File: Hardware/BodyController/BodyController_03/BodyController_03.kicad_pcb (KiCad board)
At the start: 4 copper layers, 154.9 x 116.8 mm, 332 parts, among them J1 7807, J10 7807, J11 7807, J2 CONN_01X08, J3 CONN_01X06, J5 CONN_01X14, J6 CONN_01X02, J7 CONN_01X06, J8 USB_OTG, J9 CONN_01X14, Q1 NX1029X,115, Q10 NX1029X,115, Q11 NX1029X,115, Q12 BUK9Y3R0-40E,115, Q13 BUK9Y3R0-40E,115, Q14 BUK9Y3R0-40E,115, Q15 2N7002, Q16 2N7002, Q2 NX1029X,115, Q3 BUK9Y3R0-40E,115, Q4 BUK9Y3R0-40E,115, Q5 BUK9Y3R0-40E,115, Q6 NX1029X,115, Q7 NX1029X,115, Q8 2N7002, Q9 2N7002, U1 PIC33EPxxxMU810, U10 BTS50202EKAXUMA2, U11 BTS50202EKAXUMA2, U12 BTS50202EKAXUMA2, U13 BTS50202EKAXUMA2, U14 BTS50202EKAXUMA2, U15 BTS716G, U16 MCP2562-H/SN, U17 OPA320-Q1, U18 TLV70033DDC, U19 TLV70033DDC, U2 LM2903QDRQ1, U20 LMR140x0, U21 LM2903QDRQ1, U22 UCC27511A-Q1, U23 tps25940-q1, U25 UCC27511A-Q1, U27 INA21x, U28 OPA320-Q1, U29 FT230X, U3 INA21x, U4 BTS716G, U5 BTS500801TMAATMA1, U6 BTS500801TMAATMA1, U7 BTS50202EKAXUMA2, U8 BTS50202EKAXUMA2, U9 BTS50202EKAXUMA2, Y1 8MHz

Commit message: Updated layout, cleaned up directory, and modified BOM
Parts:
- moved C59 126.1 mm to (134.0, 17.3)
- moved D15 126.1 mm to (143.3, 0.33)
- moved R112 126.1 mm to (160.7, 16.0)
- moved R115 126.1 mm to (168.1, 4.88)
- moved R119 126.1 mm to (165.0, 16.0)
- moved R12 126.1 mm to (190.8, -3.56)
- moved R159 126.1 mm to (172.3, 4.88)
- moved R17 126.1 mm to (150.3, 15.9)
- moved R2 126.1 mm to (168.1, -0.12)
- moved R7 126.1 mm to (162.3, 11.0)
- moved U17 126.1 mm to (153.1, -0.87)
- moved C20 126.1 mm to (126.5, 18.0)
- moved C10 126.1 mm to (151.7, 10.9)
- moved C14 126.1 mm to (148.0, 10.9)
- moved C19 126.1 mm to (154.4, 5.58)
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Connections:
- J5 pad 10: TURN_SIGNAL_RR_OUT -> HEATED_GRIPS_OUT
- J5 pad 11: TURN_SIGNAL_FL_OUT -> TURN_SIGNAL_RR_OUT
- J5 pad 12: TURN_SIGNAL_RL_OUT -> TURN_SIGNAL_FR_OUT
- J5 pad 3: HEADLIGHT_HI_OUT -> HEADLIGHT_LO_OUT
- J5 pad 4: HEADLIGHT_LO_OUT -> HEATED_SEAT_OUT
- J5 pad 5: HEATED_GRIPS_OUT -> TURN_SIGNAL_RL_OUT
- J5 pad 6: HEATED_SEAT_OUT -> TURN_SIGNAL_FL_OUT
- J5 pad 9: TURN_SIGNAL_FR_OUT -> HEADLIGHT_HI_OUT
- Q1 pad 2: +5P -> +3.3VP
- Q2 pad 4: +5P -> +3.3VP
- Q6 pad 4: +5P -> +3.3VP
- Q7 pad 2: +5P -> +3.3VP
- R114 pad 1: +5P -> +3.3VP
- R118 pad 1: +5P -> +3.3VP
- R133 pad 1: +5P -> +3.3VP
- R137 pad 1: +5P -> +3.3VP
- R140 pad 1: +5P -> +3.3VP
- R141 pad 1: +5P -> +3.3VP
- R146 pad 1: +5P -> +3.3VP
- R5 pad 1: +5P -> +3.3VP
- R6 pad 1: +5P -> +3.3VP
- R7 pad 1: +5P -> +3.3VP
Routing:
- net BRAKE_LIGHT_OUT: track 41.6 -> 0.00 mm
- net +12P: track 6.32 -> 37.3 mm
- net Net-(Q16-Pad2): track 0.00 -> 20.1 mm
- net +3.3VP: track 2.12 -> 19.0 mm
- net Net-(R135-Pad1): track 7.44 -> 21.6 mm
- net Net-(Q6-Pad1): track 17.1 -> 30.4 mm
- net +5P: track 7.11 -> 0.00 mm
- net GND: track 99.8 -> 104.8 mm, vias 31 -> 35
- net Net-(R30-Pad1): track 0.00 -> 3.31 mm
- net Net-(R28-Pad1): track 0.00 -> 2.95 mm
- net Net-(D27-Pad1): track 6.59 -> 9.47 mm
- net Net-(R32-Pad1): track 0.00 -> 2.65 mm
- net Net-(R29-Pad1): track 0.00 -> 2.62 mm
- net Net-(R31-Pad1): track 0.00 -> 2.53 mm
- net Net-(R27-Pad1): track 0.00 -> 2.52 mm
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- added copper zone on F.Cu, net BRAKE_LIGHT_OUT
- added copper zone on F.Cu, net HEADLIGHT_LO_OUT
- added copper zone on F.Cu, net HEATED_SEAT_OUT

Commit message: started serious layout
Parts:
- removed D17: D_Zener_15V, Diodes_SMD:D_SOD-123
- removed D20, D22: D_Schottky, Diodes_SMD:D_SOD-323
- removed D4: D_Schottky_x2_Serial_AKC, TO_SOT_Packages_SMD:SOT-23
- removed D6, D7: D, Diodes_SMD:D_SMB
- removed J10, J11: 7807, Footprints:7807
- removed J9: CONN_01X14, Connectors_Molex:Molex_MegaFit_2x06x5.70mm_Straight
- removed Q14, Q3, Q5: BUK9Y3R0-40E,115, TO_SOT_Packages_SMD:TDSON-8-1
- removed Q15: 2N7002, TO_SOT_Packages_SMD:SOT-23
- removed U17, U28: OPA320-Q1, TO_SOT_Packages_SMD:SOT-23-5
- removed U22: UCC27511A-Q1, TO_SOT_Packages_SMD:SOT-23-6
- added C100: 10nF, Capacitors_SMD:C_0603, F.Cu at (144.5, 110.8)
- added C101: 10nF, Capacitors_SMD:C_0603, F.Cu at (122.4, 170.7)
- added C102: 10nF, Capacitors_SMD:C_0603, F.Cu at (143.7, 170.7)
- added C103: 10nF, Capacitors_SMD:C_0603, F.Cu at (120.5, 171.0)
- added C104: 10nF, Capacitors_SMD:C_0603, F.Cu at (118.6, 171.0)
- added C105: 10nF, Capacitors_SMD:C_0603, F.Cu at (126.3, 171.0)
- added C106: 10nF, Capacitors_SMD:C_0603, F.Cu at (129.2, 59.8)
- added C107: 10nF, Capacitors_SMD:C_0603, F.Cu at (146.2, 61.0)
- added C108: 10nF, Capacitors_SMD:C_0603, F.Cu at (135.2, 66.0)
- added C109: 10nF, Capacitors_SMD:C_0603, F.Cu at (141.0, 66.0)
- added C110: C, Capacitors_SMD:C_0603, F.Cu at (138.0, 58.2)
- added C89: 10nF, Capacitors_SMD:C_0603, F.Cu at (150.6, 110.7)
- added C90: 10nF, Capacitors_SMD:C_0603, F.Cu at (137.9, 170.6)
- added C91: 10nF, Capacitors_SMD:C_0603, F.Cu at (141.8, 170.6)
- added C92: 10nF, Capacitors_SMD:C_0603, F.Cu at (136.0, 170.6)
- added C93: 10nF, Capacitors_SMD:C_0603, F.Cu at (130.1, 170.6)
- added C94: 10nF, Capacitors_SMD:C_0603, F.Cu at (132.1, 170.6)
- added C95: 10nF, Capacitors_SMD:C_0603, F.Cu at (156.5, 98.8)
- added C96: 10nF, Capacitors_SMD:C_0603, F.Cu at (156.5, 97.0)
- added C97: 10nF, Capacitors_SMD:C_0603, F.Cu at (134.0, 170.6)
- added C98: 10nF, Capacitors_SMD:C_0603, F.Cu at (139.8, 170.6)
- added C99: 10nF, Capacitors_SMD:C_0603, F.Cu at (147.6, 110.7)
- added J4: Conn_02x10_Top_Bottom, Footprints:34690-0200, F.Cu at (148.6, 151.1)
- added R163: 10k, Resistors_SMD:R_0603, F.Cu at (159.2, 97.0)
- added R164: 100k, Resistors_SMD:R_0603, F.Cu at (162.1, 98.8)
- added R165: 100k, Resistors_SMD:R_0603, F.Cu at (162.0, 97.0)
- added R166: 10k, Resistors_SMD:R_0603, F.Cu at (147.6, 113.8)
- added R167: 10k, Resistors_SMD:R_0603, F.Cu at (144.5, 113.8)
- added R168: 100k, Resistors_SMD:R_0603, F.Cu at (147.6, 116.6)
- added R169: 100k, Resistors_SMD:R_0603, F.Cu at (144.5, 116.6)
- added R170: 22k, Resistors_SMD:R_0603, F.Cu at (132.0, 63.2)
- added R171: 10k, Resistors_SMD:R_0603, F.Cu at (144.0, 61.8)
- added R172: 22k, Resistors_SMD:R_0603, F.Cu at (144.0, 64.5)
- C22, C57: value 10nF -> 1nF
- C58: value 2u2 -> 10nF; footprint Capacitors_SMD:C_1206 -> Capacitors_SMD:C_0603
- C59: value 4u7 -> 10nF; footprint Capacitors_SMD:C_1206 -> Capacitors_SMD:C_0603
- C60: value 1nF -> 10nF
- J1: value 7807 -> 7796; footprint Footprints:7807 -> Footprints:7796
- J2: value CONN_01X08 -> Conn_01x14; footprint Connectors_Molex:Molex_MegaFit_2x04x5.70mm_Straight -> Footprints:34772-0140
- J3: value CONN_01X06 -> Conn_02x10_Top_Bottom; footprint Connectors_Molex:Molex_MegaFit_2x03x5.70mm_Straight -> Footprints:34690-0200
- J5: value CONN_01X14 -> 7796; footprint Connectors_Molex:Molex_MegaFit_2x06x5.70mm_Straight -> Footprints:7796
- J6: value CONN_01X02 -> 7796; footprint Connectors_Molex:Molex_MegaFit_2x01x5.70mm_Straight -> Footprints:7796
- Q4: value BUK9Y3R0-40E,115 -> SQJ423EP-T1_GE3
- R10, R11, R151: value 3R -> 10k
- R112: value 100k -> 150k
- R114, R115, R116: value 100k -> 10k
- R118: value 10k -> 100k
- R119: value 1R -> 100k
- R120, R9: value 3R -> 100k
- R122, R124: value 10k -> 150k
- R156: value 0m4 -> R0005; footprint Footprints:PSR500 -> Resistors_SMD:R_2512
- R159: value 1k -> 100k
- R16: value 0m4 -> R; footprint Footprints:PSR500 -> Resistors_SMD:R_2512
- R19: value 10R -> 10k
- R56, R57: value 100R -> 10k
- R59, R60: value 100R -> 100k
- R61: value 4k7 -> 150k
- U10: value BTS50202EKAXUMA2 -> LM2904AVQDRQ1; footprint Footprints:PG_DSO_14_40_EP -> Housings_SOIC:SOIC-8_3.9x4.9mm_Pitch1.27mm
- moved C41 171.8 mm to (128.2, 170.6)
- moved C40 169.6 mm to (124.3, 170.6)
- moved D15 127.3 mm to (43.2, 79.0)
- moved R111 126.2 mm to (76.1, 69.5), turned to 270 degrees
- moved R5 123.0 mm to (76.1, 66.7), turned to 270 degrees
- moved R2 120.6 mm to (76.0, 77.8), turned to 270 degrees
- moved R125 117.8 mm to (118.7, 128.0)
- moved R126 117.8 mm to (118.7, 125.2)
- moved R127 117.8 mm to (118.7, 122.4)
- moved R128 117.3 mm to (116.8, 122.4)
- moved R129 117.3 mm to (112.8, 122.4)
- moved C67 117.2 mm to (114.8, 122.4)
- moved U23 117.2 mm to (114.8, 127.1)
- moved C21 116.1 mm to (63.2, 82.3)
- moved R8 115.8 mm to (87.2, 78.5)
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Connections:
- net 12P_MONITOR renamed 12P_MONITOR_AI
- net 12V_MONITOR renamed 12V_MONITOR_AI
- net AUX_PORT_ISENSE renamed AUX_PORT_ISENSE_AI
- net BATT_ISENSE renamed BATT_ISENSE_AI
- net DCDC_ISENSE renamed DCDC_ISENSE_AI
- net ECU_1_ISENSE renamed ECU_1_ISENSE_AI
- net ECU_2_ISENSE renamed ECU_2_ISENSE_AI
- net FAN_ISENSE renamed FAN_ISENSE_AI
- net HEADLIGHT_ISENSE renamed HEADLIGHT_ISENSE_AI
- net HEATER_ISENSE renamed HEATER_ISENSE_AI
- net HORN_ISENSE renamed HORN_ISENSE_AI
- net IC_CONTROLLER_ISENSE renamed IC_CONTROLLER_ISENSE_AI
- net LOCK_ISENSE renamed LOCK_ISENSE_AI
- net TAILLIGHT_ISENSE renamed TAILLIGHT_ISENSE_AI
- C22 pad 1: +3.3VP -> GND
- C22 pad 2: GND -> Net-(C22-Pad2)
- C36 pad 1: PUMP_ISENSE -> THROTTLE_SIGNAL_MONITOR_AI
- C47 pad 1: +5V -> +12V
- C57 pad 1: +12P -> GND
- C57 pad 2: GND -> Net-(C57-Pad2)
- C58 pad 1: Net-(C58-Pad1) -> TURN_LEFT_SWITCH_IN
- C58 pad 2: Net-(C58-Pad2) -> GND
- C59 pad 1: /TopLevel/PowerInput/ChargePump -> TURN_RIGHT_SWITCH_IN
- C59 pad 2: +12P -> GND
- C60 pad 1: Net-(C60-Pad1) -> BRIGHTS_SWITCH_IN
- C64 pad 1: FAN_SPEED_2_OUT -> BRAKE_SWITCH_1_IN
- C66 pad 1: PUMP_SPEED_2_OUT -> BRAKE_SWITCH_2_IN
- C82 pad 1: +3.3VP -> HORN_SWITCH_IN
- D18 pad 1: FAN_2_OUT -> PUMP_1_OUT
- D8 pad 1: Net-(D8-Pad1) -> /TopLevel/PowerInput/BATT_SHUNT
- J2 pad 1: CHARGE_PORT_RELEASE_OUT -> BRAKE_LIGHT_OUT
- J2 pad 2: STEERING_COLUMN_LOCK_OUT -> TAILLIGHT_OUT
- J2 pad 3: Net-(J2-Pad3) -> HEADLIGHT_LO_OUT
- J2 pad 4: DCDC_CONTACTOR_OUT -> HEADLIGHT_HI_OUT
- J2 pad 5: BATTERY_CONTACTOR_OUT -> HEATED_SEAT_OUT
- J2 pad 6: PRECHARGE_RELAY_OUT -> HEATED_GRIPS_OUT
- J2 pad 7: CHARGER_CONTACTOR_OUT -> TURN_SIGNAL_RL_OUT
- J2 pad 8: Net-(J2-Pad8) -> TURN_SIGNAL_FL_OUT
- J3 pad 1: BMS_CONTROLLER_OUT -> PUMP_1_OUT
- J3 pad 2: IC_CONTROLLER_OUT -> FAN_1_OUT
- J3 pad 3: MOTOR_CONTROLLER_OUT -> CHARGE_CONTROLLER_OUT
- J3 pad 4: CHARGE_CONTROLLER_OUT -> MOTOR_CONTROLLER_OUT
- J3 pad 6: Net-(J3-Pad6) -> BMS_CONTROLLER_OUT
- J5 pad 1: AUX_PORT_OUT -> DCDC
- J6 pad 1: CAN_P -> GND
- Q1 pad 1: Net-(Q1-Pad1) -> Net-(C22-Pad2)
- Q1 pad 3: +BATT -> Net-(D8-Pad2)
- Q1 pad 4: Net-(D8-Pad1) -> /TopLevel/PowerInput/BATT_SHUNT
- Q1 pad 5: Net-(D8-Pad2) -> Net-(Q1-Pad5)
- Q1 pad 6: Net-(D22-Pad1) -> Net-(Q1-Pad6)
- Q2 pad 1: Net-(Q1-Pad1) -> Net-(C22-Pad2)
- Q4 pad 1: +BATT -> /TopLevel/PowerInput/BATT_SHUNT
- Q4 pad 2: +BATT -> /TopLevel/PowerInput/BATT_SHUNT
- Q4 pad 3: +BATT -> /TopLevel/PowerInput/BATT_SHUNT
- Q4 pad 4: Net-(Q4-Pad4) -> Net-(D8-Pad2)
- Q4 pad 5: Net-(Q3-Pad5) -> +BATT
- Q6 pad 1: Net-(Q6-Pad1) -> Net-(C57-Pad2)
- Q7 pad 1: Net-(Q6-Pad1) -> Net-(C57-Pad2)
- R10 pad 1: Net-(R10-Pad1) -> Net-(Q1-Pad5)
- R10 pad 2: Net-(Q4-Pad4) -> Net-(Q1-Pad6)
- R11 pad 1: Net-(R10-Pad1) -> TURN_LEFT_SWITCH
- R11 pad 2: Net-(Q5-Pad4) -> TURN_LEFT_SWITCH_IN
- R111 pad 1: Net-(Q1-Pad1) -> Net-(C22-Pad2)
- R112 pad 1: Net-(D8-Pad1) -> DAC_PWM_2
- R112 pad 2: Net-(D8-Pad2) -> Net-(C107-Pad2)
- R113 pad 2: Net-(D22-Pad2) -> GND
- R114 pad 1: +3.3VP -> BRIGHTS_SWITCH
- R114 pad 2: Net-(R114-Pad2) -> BRIGHTS_SWITCH_IN
- R115 pad 1: Net-(R114-Pad2) -> HORN_SWITCH
- R115 pad 2: GND -> HORN_SWITCH_IN
- R116 pad 1: Net-(R116-Pad1) -> KICKSTAND_SWITCH
- R116 pad 2: Net-(R114-Pad2) -> KICKSTAND_SWITCH_IN
- R117 pad 1: Net-(R116-Pad1) -> +3.3VP
- R117 pad 2: Net-(C60-Pad1) -> TURN_LEFT_SWITCH
- R118 pad 2: Net-(R116-Pad1) -> BRAKE_SWITCH_1
- R119 pad 1: Net-(C58-Pad2) -> +3.3VP
- R119 pad 2: Net-(R119-Pad2) -> BRIGHTS_SWITCH
- R120 pad 1: Net-(C58-Pad2) -> +3.3VP
- R120 pad 2: Net-(R120-Pad2) -> HORN_SWITCH
- R122 pad 1: FAN_SPEED_2_OUT -> Net-(C106-Pad2)
- R122 pad 2: FAN_SPEED_2_PWM -> Net-(C108-Pad1)
- R124 pad 1: PUMP_SPEED_2_OUT -> Net-(C107-Pad2)
- R124 pad 2: PUMP_SPEED_2_PWM -> Net-(C109-Pad1)
- R139 pad 1: Net-(Q6-Pad1) -> Net-(C57-Pad2)
- R14 pad 1: Net-(R14-Pad1) -> +12V
- R140 pad 2: Net-(Q6-Pad1) -> Net-(C57-Pad2)
- R15 pad 1: Net-(R15-Pad1) -> /TopLevel/PowerInput/BATT_SHUNT
- R151 pad 1: Net-(R148-Pad2) -> Net-(R151-Pad1)
- R151 pad 2: Net-(Q14-Pad4) -> DAC_OUT_1
- R154 pad 1: Net-(R154-Pad1) -> +12V
- R155 pad 1: Net-(R155-Pad1) -> Net-(Q12-Pad5)
- R156 pad 2: Net-(R154-Pad1) -> Net-(Q12-Pad5)
- R159 pad 1: /TopLevel/PowerInput/ChargePump -> +3.3VP
- R159 pad 2: Net-(D8-Pad1) -> KICKSTAND_SWITCH
- R16 pad 2: Net-(R14-Pad1) -> /TopLevel/PowerInput/BATT_SHUNT
- R161 pad 1: Net-(D8-Pad2) -> SPARE_SWITCH_1
- R161 pad 2: Net-(D20-Pad2) -> SPARE_SWITCH_1_IN
- R19 pad 1: Net-(D8-Pad1) -> TURN_RIGHT_SWITCH
- R19 pad 2: Net-(R10-Pad1) -> TURN_RIGHT_SWITCH_IN
- R20 pad 2: FAN_2_EN -> PUMP_1_EN
- R5 pad 2: Net-(Q1-Pad1) -> Net-(C22-Pad2)
- R56 pad 1: Net-(R56-Pad1) -> THROTTLE_SIGNAL
- R56 pad 2: PUMP_2_EN -> THROTTLE_SIGNAL_MONITOR_AI
- R57 pad 1: Net-(R57-Pad1) -> BRAKE_SWITCH_1
- R57 pad 2: DIAG_SELECT -> BRAKE_SWITCH_1_IN
- R58 pad 1: Net-(R58-Pad1) -> BRAKE_SWITCH_2
- R58 pad 2: PUMP_ISENSE -> BRAKE_SWITCH_2_IN
- R59 pad 1: Net-(R59-Pad1) -> +3.3VP
- R59 pad 2: PUMP_1_EN -> BRAKE_SWITCH_2
- R60 pad 1: Net-(R60-Pad1) -> +3.3VP
- R60 pad 2: DIAG_EN -> TURN_RIGHT_SWITCH
- R61 pad 1: GND -> DAC_PWM_1
- R61 pad 2: Net-(R58-Pad1) -> Net-(C106-Pad2)
- R9 pad 1: Net-(R10-Pad1) -> /TopLevel/PowerInput/BATT_SHUNT
- R9 pad 2: Net-(Q3-Pad4) -> Net-(Q1-Pad5)
- U1 pad 19: IC_CONTROLLER_~FLT -> BATT_~FAULT
- U1 pad 24: PUMP_ISENSE -> THROTTLE_SIGNAL_MONITOR_AI
- U1 pad 39: FAN_2_EN -> BRAKE_SWITCH_1_IN
- U1 pad 40: Net-(U1-Pad40) -> BRAKE_SWITCH_2_IN
- U1 pad 49: PUMP_1_EN -> DAC_PWM_1
- U1 pad 5: BATT_~FAULT -> IC_CONTROLLER_~FLT
- U1 pad 50: PUMP_2_EN -> DAC_PWM_2
- U1 pad 51: PUMP_SPEED_2_PWM -> FAN_1_EN
- U1 pad 52: PUMP_SPEED_1_PWM -> PUMP_1_EN
- U1 pad 53: FAN_1_EN -> Net-(U1-Pad53)
- U1 pad 56: Net-(U1-Pad56) -> TURN_RIGHT_SWITCH_IN
- U1 pad 57: Net-(U1-Pad57) -> TURN_LEFT_SWITCH_IN
- U1 pad 59: IC_CONTROLLER_SLEEP -> Net-(U1-Pad59)
- U1 pad 7: Net-(U1-Pad7) -> SPARE_SWITCH_1_IN
- U1 pad 8: Net-(U1-Pad8) -> SPARE_SWITCH_2_IN
- U1 pad 88: FAN_SPEED_2_PWM -> PUMP_SPEED_1_PWM
- U1 pad 89: Net-(U1-Pad89) -> KILL_SWITCH_IN
- U1 pad 90: Net-(U1-Pad90) -> IGNITION_SWITCH_IN
- U1 pad 95: Net-(U1-Pad95) -> KICKSTAND_SWITCH_IN
- U1 pad 96: Net-(U1-Pad96) -> BRIGHTS_SWITCH_IN
- U1 pad 97: Net-(U1-Pad97) -> HORN_SWITCH_IN
- U10 pad 1: GND -> DAC_OUT_1
- U10 pad 2: Net-(R59-Pad1) -> Net-(R151-Pad1)
- U10 pad 3: Net-(R60-Pad1) -> Net-(C108-Pad1)
- U10 pad 4: Net-(R58-Pad1) -> GND
- U10 pad 5: Net-(R57-Pad1) -> Net-(C109-Pad1)
- U10 pad 6: Net-(R56-Pad1) -> Net-(R171-Pad1)
- U10 pad 7: Net-(U10-Pad7) -> DAC_OUT_2
- U10 pad 8: PUMP_2_OUT -> +12P
- U11 pad 10: FAN_2_OUT -> PUMP_1_OUT
- U11 pad 8: FAN_2_OUT -> PUMP_1_OUT
- U11 pad 9: FAN_2_OUT -> PUMP_1_OUT
- U15 pad 6: Net-(U15-Pad6) -> GND
- U19 pad 1: +5V -> +12V
- U2 pad 1: Net-(Q1-Pad1) -> Net-(C22-Pad2)
- U2 pad 5: Net-(R114-Pad2) -> Net-(U2-Pad5)
- U2 pad 6: Net-(C60-Pad1) -> Net-(U2-Pad6)
- U2 pad 7: Net-(R116-Pad1) -> Net-(U2-Pad7)
- U21 pad 1: Net-(Q6-Pad1) -> Net-(C57-Pad2)
- U27 pad 1: Net-(U27-Pad1) -> Net-(C79-Pad1)
- U3 pad 1: Net-(U17-Pad1) -> Net-(C19-Pad1)
- U4 pad 6: Net-(U4-Pad6) -> GND
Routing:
- net DIAG_SELECT: track 0.00 -> 139.4 mm, vias 0 -> 9
- net Net-(R33-Pad1): track 0.00 -> 138.8 mm, vias 0 -> 2
- net Net-(R34-Pad1): track 12.5 -> 135.6 mm, vias 0 -> 2
- net Net-(R39-Pad1): track 0.00 -> 121.7 mm, vias 0 -> 4
- net DIAG_EN: track 0.00 -> 114.9 mm, vias 0 -> 8
- net CONTACT_1_2_STATUS: track 0.00 -> 113.8 mm, vias 0 -> 4
- net Net-(R42-Pad1): track 0.00 -> 110.2 mm, vias 0 -> 4
- net AUX_PORT_EN: track 0.00 -> 108.0 mm, vias 0 -> 2
- net Net-(R45-Pad1): track 0.00 -> 105.0 mm, vias 0 -> 4
- net HORN_EN: track 2.09 -> 103.0 mm, vias 0 -> 2
- net CONTACT_3_4_STATUS: track 0.00 -> 100.8 mm, vias 0 -> 4
- net Net-(R22-Pad1): track 0.00 -> 96.7 mm, vias 0 -> 2
- net BRAKE_LIGHT_EN: track 0.00 -> 87.6 mm, vias 0 -> 2
- net HEATED_SEAT_EN: track 0.00 -> 82.9 mm, vias 0 -> 2
- net STEERING_COLUMN_LOCK_EN: track 0.00 -> 82.2 mm, vias 0 -> 2
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- removed copper zone on F.Cu, net +12V
- removed copper zone on F.Cu, net +BATT
- removed copper zone on F.Cu, net BRAKE_LIGHT_OUT
- removed copper zone on F.Cu, net DCDC
- removed copper zone on F.Cu, net HEADLIGHT_LO_OUT
- removed copper zone on F.Cu, net HEATED_SEAT_OUT
- removed copper zone on F.Cu, net Net-(Q12-Pad5)
- removed copper zone on F.Cu, net Net-(Q3-Pad5)
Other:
- board size 154.9 x 116.8 mm -> 155 x 117 mm
- net class 5A: trace_width 4 -> 2
- board text added: "12V_SW"
- board text added: "5V_MAIN"
- board text added: "B+"
- board text added: "CAN"
- board text added: "DAC"
- board text added: "DCDC"
- board text added: "GND"

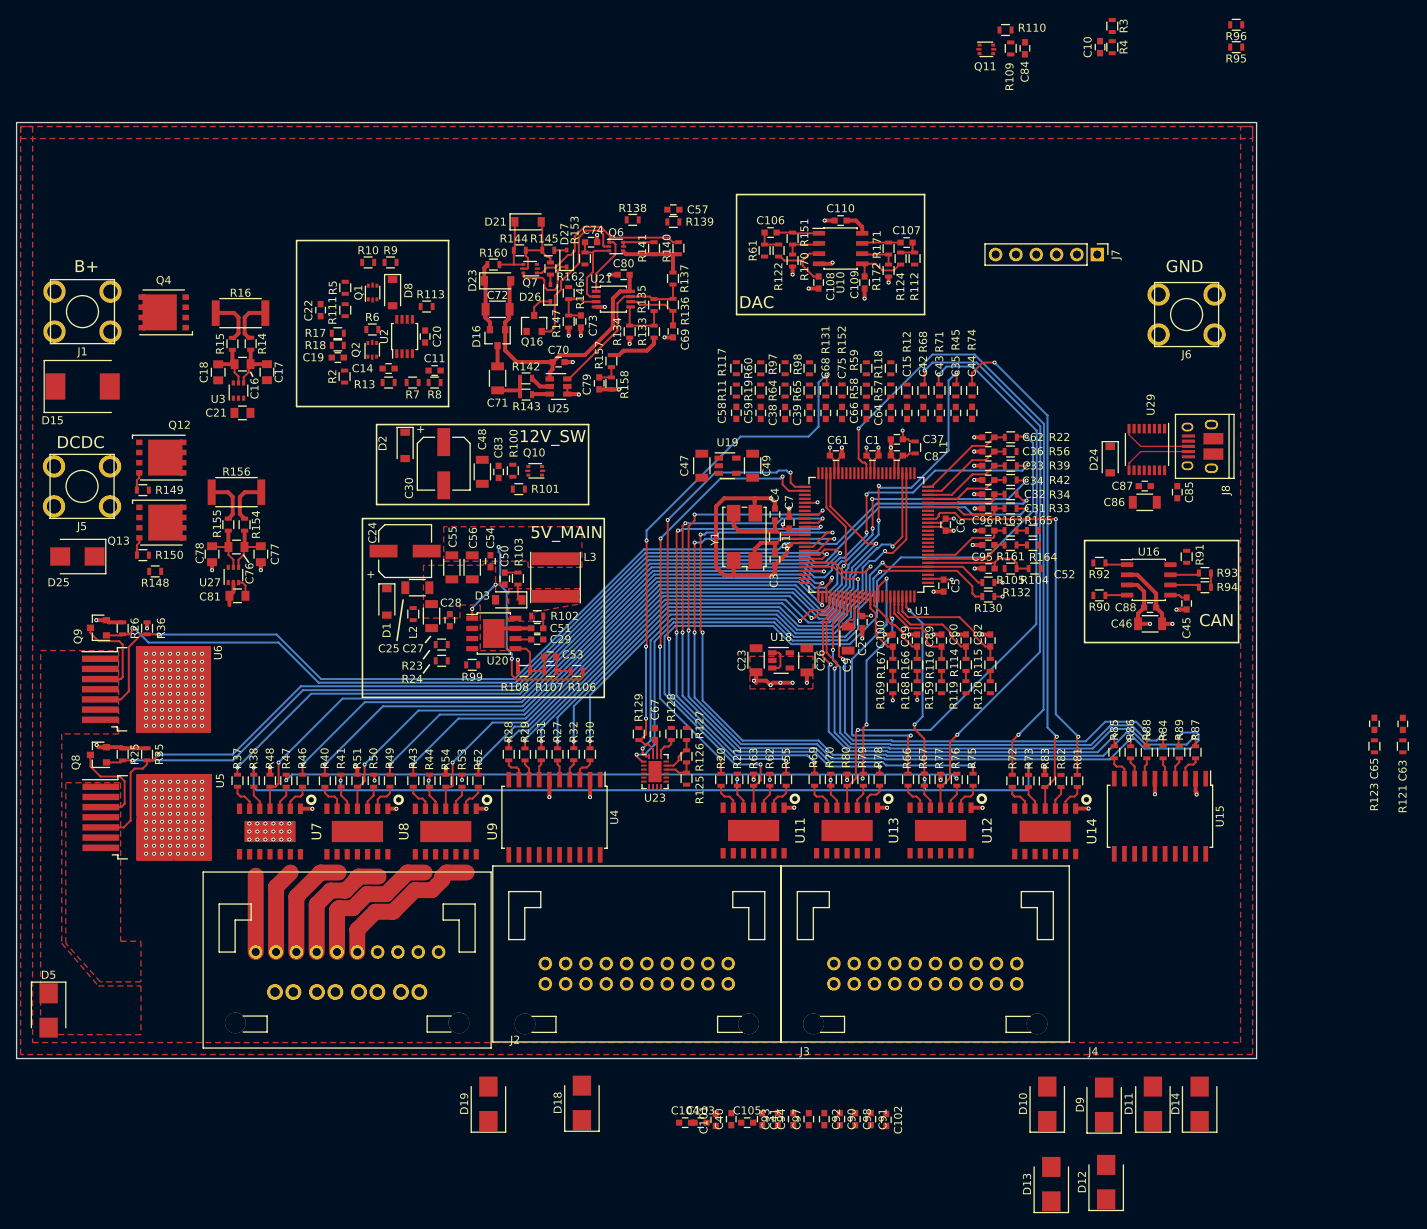
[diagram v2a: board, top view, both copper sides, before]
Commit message: Body Controller Layout Done
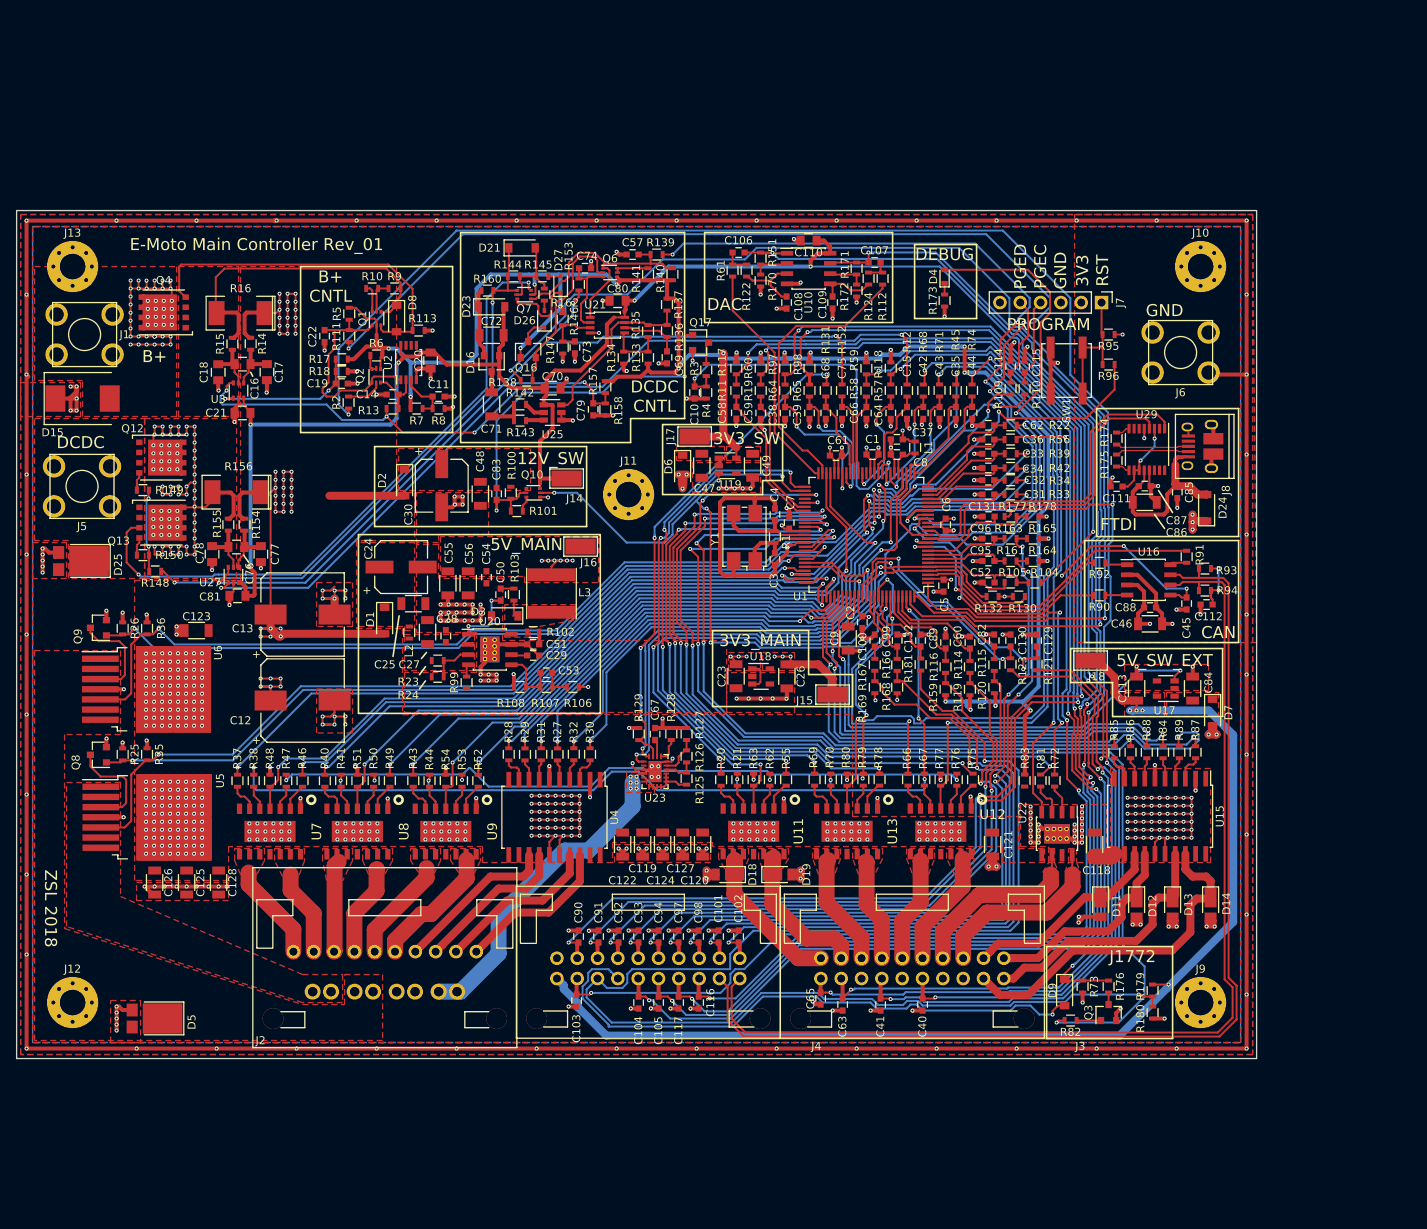
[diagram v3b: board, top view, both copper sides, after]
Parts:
- removed D10: D, Diodes_SMD:D_SMB
- removed Q11: NX1029X,115, TO_SOT_Packages_SMD:SOT-666
- removed U14: BTS50202EKAXUMA2, Footprints:PG_DSO_14_40_EP
- added C111: 100nF, Capacitors_SMD:C_0603, F.Cu at (172.5, 91.5)
- added C112: 10nF, Capacitors_SMD:C_0603, F.Cu at (183.8, 106.2)
- added C113: 10uF, Capacitors_SMD:C_1206, F.Cu at (175.0, 116.8)
- added C114: 10nF, Capacitors_SMD:C_0603, F.Cu at (159.2, 76.5)
- added C115: 10nF, Capacitors_SMD:C_0603, F.Cu at (161.0, 76.5)
- added C116: 10nF, Capacitors_SMD:C_0603, F.Cu at (120.2, 156.0)
- added C117: 10nF, Capacitors_SMD:C_0603, F.Cu at (117.8, 156.0)
- added C118: 10uF, Capacitors_SMD:C_1206, F.Cu at (169.8, 136.2)
- added C119: 10uF, Capacitors_SMD:C_1206, F.Cu at (113.2, 136.2)
- added C12: 470uF, Capacitors_SMD:CP_Elec_10x10, F.Cu at (70.8, 118.2)
- added C120: 10uF, Capacitors_SMD:C_1206, F.Cu at (120.8, 136.2)
- added C121: 10uF, Capacitors_SMD:C_1206, F.Cu at (157.0, 136.2)
- added C122: 10uF, Capacitors_SMD:C_1206, F.Cu at (110.8, 136.2)
- added C123: 10uF, Capacitors_SMD:C_1206, F.Cu at (57.5, 109.5)
- added C124: 10uF, Capacitors_SMD:C_1206, F.Cu at (115.8, 136.2)
- added C125: 10uF, Capacitors_SMD:C_1206, F.Cu at (56.2, 141.0)
- added C126: 10uF, Capacitors_SMD:C_1206, F.Cu at (52.2, 141.0)
- added C127: 10uF, Capacitors_SMD:C_1206, F.Cu at (118.2, 136.2)
- added C128: 10uF, Capacitors_SMD:C_1206, F.Cu at (60.2, 141.0)
- added C129: 10nF, Capacitors_SMD:C_0603, F.Cu at (162.5, 110.8)
- added C13: 470uF, Capacitors_SMD:CP_Elec_10x10, F.Cu at (70.8, 107.5)
- added C130: 10nF, Capacitors_SMD:C_0603, F.Cu at (159.2, 110.8)
- added C131: 10nF, Capacitors_SMD:C_0603, F.Cu at (156.5, 95.2)
- added C132: 10nF, Capacitors_SMD:C_0603, F.Cu at (148.0, 110.8)
- added D4: D_LED, Diodes_SMD:D_0603, F.Cu at (151.0, 65.2)
- added D6: D_Schottky, Diodes_SMD:D_SOD-123, F.Cu at (118.2, 89.2)
- added D7: D_Schottky, Diodes_SMD:D_SOD-123, F.Cu at (184.5, 119.8)
- added J10: Conn_01x01, Mounting_Holes:MountingHole_3.2mm_M3_Pad_Via, F.Cu at (183.0, 64.0)
- added J11: Conn_01x01, Mounting_Holes:MountingHole_3.2mm_M3_Pad_Via, F.Cu at (111.5, 92.5)
- added J12: Conn_01x01, Mounting_Holes:MountingHole_3.2mm_M3_Pad_Via, F.Cu at (42.0, 156.0)
- added J13: Conn_01x01, Mounting_Holes:MountingHole_3.2mm_M3_Pad_Via, F.Cu at (42.0, 64.0)
- added J14: TEST_1P, Measurement_Points:Test_Point_Keystone_5019_Minature, F.Cu at (103.8, 90.5)
- added J15: TEST_1P, Measurement_Points:Test_Point_Keystone_5019_Minature, F.Cu at (137.0, 117.5)
- added J16: TEST_1P, Measurement_Points:Test_Point_Keystone_5019_Minature, F.Cu at (105.5, 99.0)
- added J17: TEST_1P, Measurement_Points:Test_Point_Keystone_5019_Minature, F.Cu at (119.8, 85.2)
- added J18: TEST_1P, Measurement_Points:Test_Point_Keystone_5019_Minature, F.Cu at (169.2, 113.2)
- added J9: Conn_01x01, Mounting_Holes:MountingHole_3.2mm_M3_Pad_Via, F.Cu at (183.0, 156.0)
- added NT1: Net_Tie-0.5mm, Footprints:Net_Tie-0.5mm, F.Cu at (61.0, 69.8)
- added NT2: Net_Tie-0.5mm, Footprints:Net_Tie-0.5mm, F.Cu at (65.0, 69.8)
- added NT3: Net_Tie-0.5mm, Footprints:Net_Tie-0.5mm, F.Cu at (60.5, 92.2)
- added NT4: Net_Tie-0.5mm, Footprints:Net_Tie-0.5mm, F.Cu at (64.5, 92.2)
- added Q17: Q_PMOS_GSD, TO_SOT_Packages_SMD:SOT-23, F.Cu at (120.5, 73.5)
- added Q3: 2N7002, TO_SOT_Packages_SMD:SOT-23, F.Cu at (171.5, 157.2)
- added R173: 100R, Resistors_SMD:R_0603, F.Cu at (151.0, 68.2)
- added R174: 22R, Resistors_SMD:R_0603, F.Cu at (172.5, 85.5)
- added R175: 22R, Resistors_SMD:R_0603, F.Cu at (172.5, 88.2)
- added R176: R, Resistors_SMD:R_0603, F.Cu at (171.5, 154.0)
- added R177: R, Resistors_SMD:R_0603, F.Cu at (159.2, 95.2)
- added R178: R, Resistors_SMD:R_0603, F.Cu at (162.0, 95.2)
- added R179: R, Resistors_SMD:R_0603, F.Cu at (177.0, 154.5)
- added R180: R, Resistors_SMD:R_0603, F.Cu at (177.0, 157.2)
- added R181: R, Resistors_SMD:R_0603, F.Cu at (148.0, 113.8)
- added SW1: PTS645SM43SMTR92 LFS, Buttons_Switches_SMD:SW_SPST_EVQP0, F.Cu at (166.2, 77.0)
- added U17: TPS70950QDBVRQ1, TO_SOT_Packages_SMD:SOT-23-5, F.Cu at (178.7, 116.8)
- added U22: DRV8872DDARQ1, Housings_SOIC:HTSOP-8-1EP_3.9x4.9mm_Pitch1.27mm_ThermalVias, F.Cu at (165.1, 134.9)
- C110: value C -> 1uF; footprint Capacitors_SMD:C_0603 -> Capacitors_SMD:C_0805
- C20, C70, C80: value 10nF -> 1uF; footprint Capacitors_SMD:C_0603 -> Capacitors_SMD:C_0805
- C84: value 100nF -> 10uF; footprint Capacitors_SMD:C_0603 -> Capacitors_SMD:C_1206
- D11, D12, D13, D14, D18, D19: footprint Diodes_SMD:D_SMB -> Diodes_SMD:D_PowerDI-123
- D25, D5: footprint Diodes_SMD:D_SMB -> Footprints:SOT1289
- D9: value D -> D_Schottky; footprint Diodes_SMD:D_SMB -> Diodes_SMD:D_SOD-123
- R109: value 100k -> 100R
- R110: value 10k -> 100R
- R156, R16: footprint Resistors_SMD:R_2512 -> SMD_Packages:SMD-2512_Pol
- R73, R82: value 100R -> R
- U18, U19: value TLV70033DDC -> TPS70933QDBVRQ1
- U20: footprint Housings_SOIC:Diodes_PSOP-8 -> Housings_SOIC:HTSOP-8-1EP_3.9x4.9mm_Pitch1.27mm_ThermalVias
- moved C84 82.7 mm to (182.0, 116.8)
- moved C63 78.3 mm to (138.2, 156.2), turned to 270 degrees
- moved C65 77.3 mm to (135.5, 155.5), turned to 270 degrees
- moved R4 66.6 mm to (121.2, 79.8)
- moved C10 66.6 mm to (119.8, 79.8)
- moved R3 66.5 mm to (121.2, 76.9)
- moved R121 46.9 mm to (162.5, 113.7)
- moved R123 46.6 mm to (159.2, 113.7)
- moved D19 46.3 mm to (130.3, 140.0), turned to 0 degrees
- moved R96 45.4 mm to (171.5, 76.2)
- moved R110 44.9 mm to (161.0, 79.2), turned to 270 degrees
- moved R109 42.5 mm to (159.2, 79.2), turned to 270 degrees
- moved C91 41.0 mm to (107.8, 147.8), turned to 90 degrees
- moved C90 39.8 mm to (105.2, 147.8), turned to 90 degrees
- moved R95 39.3 mm to (171.5, 72.5)
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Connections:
- C20 pad 1: +12P -> GND
- C20 pad 2: GND -> +12P
- C47 pad 1: +12V -> Net-(C47-Pad1)
- C70 pad 1: +12P -> GND
- C70 pad 2: GND -> +12P
- C80 pad 1: +12P -> GND
- C80 pad 2: GND -> +12P
- C84 pad 1: +5V -> Net-(C84-Pad1)
- C84 pad 2: Net-(C84-Pad2) -> GND
- D9 pad 1: STEERING_COLUMN_LOCK_OUT -> Net-(D9-Pad1)
- D9 pad 2: GND -> PILOT_IN
- J2 pad 11: HORN_OUT -> AUX_PORT_OUT
- J2 pad 12: AUX_PORT_OUT -> HORN_OUT
- J2 pad 13: Net-(J2-Pad13) -> GND
- J2 pad 14: Net-(J2-Pad14) -> IC_CONTROLLER_OUT
- J3 pad 11: BATTERY_CONTACTOR_OUT -> PUMP_SPEED_1_OUT
- J3 pad 12: DCDC_CONTACTOR_OUT -> FAN_SPEED_1_OUT
- J3 pad 13: Net-(J3-Pad13) -> GND
- J3 pad 14: Net-(J3-Pad14) -> RADIATOR_INPUT_TEMP_OUT
- J3 pad 15: Net-(J3-Pad15) -> GND
- J3 pad 16: Net-(J3-Pad16) -> RADIATOR_OUTPUT_TEMP_OUT
- J3 pad 17: Net-(J3-Pad17) -> GND
- J3 pad 18: Net-(J3-Pad18) -> GND
- J3 pad 19: Net-(J3-Pad19) -> DCDC_CONTACTOR_OUT
- J3 pad 20: Net-(J3-Pad20) -> BATTERY_CONTACTOR_OUT
- J4 pad 1: IC_CONTROLLER_OUT -> GND
- J4 pad 11: Net-(J4-Pad11) -> +5VP
- J4 pad 13: BRAKE_SWITCH_1 -> PROXIMITY_IN
- J4 pad 14: BRAKE_SWITCH_2 -> PILOT_IN
- J4 pad 15: DAC_OUT_1 -> BRAKE_SWITCH_1
- J4 pad 16: DAC_OUT_2 -> BRAKE_SWITCH_2
- J4 pad 17: Net-(J4-Pad17) -> DAC_OUT_1
- J4 pad 18: Net-(J4-Pad18) -> DAC_OUT_2
- J7 pad 4: PGEC -> Net-(C115-Pad1)
- J7 pad 5: PGED -> Net-(C114-Pad1)
- Q12 pad 5: Net-(Q12-Pad5) -> /TopLevel/DCDC/DCDC_SHUNT
- Q13 pad 5: Net-(Q12-Pad5) -> /TopLevel/DCDC/DCDC_SHUNT
- R109 pad 1: +5V -> Net-(C114-Pad1)
- R109 pad 2: Net-(C84-Pad2) -> PGEC
- R110 pad 1: Net-(C84-Pad2) -> Net-(C115-Pad1)
- R110 pad 2: Net-(Q11-Pad6) -> PGED
- R14 pad 1: +12V -> Net-(NT2-Pad2)
- R15 pad 1: /TopLevel/PowerInput/BATT_SHUNT -> Net-(NT1-Pad2)
- R154 pad 1: +12V -> Net-(NT4-Pad2)
- R155 pad 1: Net-(Q12-Pad5) -> Net-(NT3-Pad2)
- R156 pad 2: Net-(Q12-Pad5) -> /TopLevel/DCDC/DCDC_SHUNT
- R73 pad 1: Net-(R73-Pad1) -> Net-(D9-Pad1)
- R73 pad 2: DIAG_SELECT -> GND
- R82 pad 2: DIAG_EN -> PILOT_EN
- R83 pad 1: GND -> +3.3VP
- U1 pad 1: Net-(U1-Pad1) -> STEERING_COLUMN_LOCK_EN
- U1 pad 17: CHARGE_PORT_RELEASE_EN -> DEBUG_LED
- U1 pad 38: STEERING_COLUMN_LOCK_EN -> Net-(U1-Pad38)
- U1 pad 49: DAC_PWM_1 -> DAC_PWM_2
- U1 pad 50: DAC_PWM_2 -> DAC_PWM_1
- U1 pad 53: Net-(U1-Pad53) -> CHARGE_PORT_RELEASE_EN
- U1 pad 59: Net-(U1-Pad59) -> PILOT_EN
- U1 pad 9: Net-(U1-Pad9) -> PILOT_MONITOR_AI
- U1 pad 92: Net-(U1-Pad92) -> PROXIMITY_MONITOR_AI
- U19 pad 1: +12V -> Net-(C47-Pad1)
- U29 pad 8: USB_D+ -> Net-(R174-Pad2)
- U29 pad 9: USB_D- -> Net-(R175-Pad2)
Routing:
- net GND: track 151.5 -> 940.4 mm, vias 70 -> 311
- net +3.3VP: track 16.1 -> 259.6 mm, vias 0 -> 22
- net +12V: track 11.7 -> 222.8 mm, vias 178 -> 420
- net +12P: track 40.4 -> 220.1 mm, vias 0 -> 6
- net BATT_EN: track 0.00 -> 178.0 mm, vias 0 -> 2
- net DAC_OUT_1: track 5.34 -> 182.4 mm, vias 0 -> 4
- net PROXIMITY_IN: track 0.00 -> 176.9 mm, vias 0 -> 2
- net TURN_LEFT_SWITCH: track 0.00 -> 174.1 mm, vias 0 -> 4
- net TURN_RIGHT_SWITCH: track 0.00 -> 168.1 mm, vias 0 -> 4
- net DAC_OUT_2: track 4.85 -> 165.1 mm, vias 0 -> 4
- net BRAKE_SWITCH_2: track 0.00 -> 159.9 mm, vias 0 -> 4
- net BRAKE_SWITCH_1: track 0.00 -> 159.7 mm, vias 0 -> 4
- net RADIATOR_INPUT_TEMP_OUT: track 0.00 -> 151.6 mm, vias 0 -> 4
- net BATT_~FAULT: track 0.00 -> 149.1 mm, vias 0 -> 4
- net DCDC_EN: track 0.00 -> 146.5 mm, vias 0 -> 2
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- added copper zone on F.Cu, net +12V
- added copper zone on F.Cu, net +3.3VP
- added copper zone on F.Cu, net +3V3
- added copper zone on In2.Cu, net +5V
- added copper zone on F.Cu, net +5VP
- added copper zone on F.Cu, net +BATT
- added copper zone on In2.Cu, net +BATT
- added copper zone on F.Cu, net /TopLevel/DCDC/DCDC_SHUNT
- added copper zone on In2.Cu, net /TopLevel/DCDC/DCDC_SHUNT
- added copper zone on F.Cu, net /TopLevel/PowerInput/BATT_SHUNT
- added copper zone on F.Cu, net /TopLevel/PowerRails/buck_holdup
- added copper zone on F.Cu, net /TopLevel/PowerRails/buck_input
- added copper zone on F.Cu, net BMS_CONTROLLER_OUT
- added copper zone on F.Cu, net BRAKE_LIGHT_OUT
- added copper zone on F.Cu, net CHARGE_CONTROLLER_OUT
- added copper zone on F.Cu, net CHARGE_PORT_RELEASE_OUT
- added copper zone on F.Cu, net DCDC
- added copper zone on F.Cu, net FAN_1_OUT
- added copper zone on B.Cu, net GND
- added copper zone on In2.Cu, net GND
- added copper zone on F.Cu, net HEADLIGHT_HI_OUT
- added copper zone on F.Cu, net HEADLIGHT_LO_OUT
- added copper zone on F.Cu, net HEATED_GRIPS_OUT
- added copper zone on F.Cu, net HEATED_SEAT_OUT
- added copper zone on F.Cu, net IC_CONTROLLER_OUT
- added copper zone on F.Cu, net J1772_CONTROLLER_OUT
- added copper zone on F.Cu, net MOTOR_CONTROLLER_OUT
- added copper zone on F.Cu, net Net-(C30-Pad1)
- added copper zone on F.Cu, net Net-(C47-Pad1)
- added copper zone on F.Cu, net Net-(C84-Pad1)
- added copper zone on F.Cu, net PUMP_1_OUT
- added copper zone on F.Cu, net STEERING_COLUMN_LOCK_OUT
- added copper zone on F.Cu, net TAILLIGHT_OUT
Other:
- board size 155 x 117 mm -> 155 x 106 mm
- board text added: "3V3"
- board text added: "3V3_MAIN"
- board text added: "3V3_SW"
- board text added: "5V_SW_EXT"
- board text added: "B+ CNTL"
- board text added: "DCDC CNTL"
- board text added: "DEBUG"
- board text added: "E-Moto Main Controller Rev_01"
- board text added: "FTDI"
- board text added: "J1772"
- board text added: "PGEC"
- board text added: "PGED"
- board text added: "PROGRAM"
- board text added: "RST"
- board text added: "ZSL 2018"
